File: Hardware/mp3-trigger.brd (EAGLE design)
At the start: 58.4 x 62.2 mm, 88 parts, among them IC1 LM1117, J1 POWER_JACKTOE, Q1 12.288MHz, U1 CY8C29466, U10 M18_, U2 USD-SOCKET, U3 MUX-74HC4067SMD, U5 1.8V Reg, U6 NAV_SWITCHSMD, U7 VS1063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

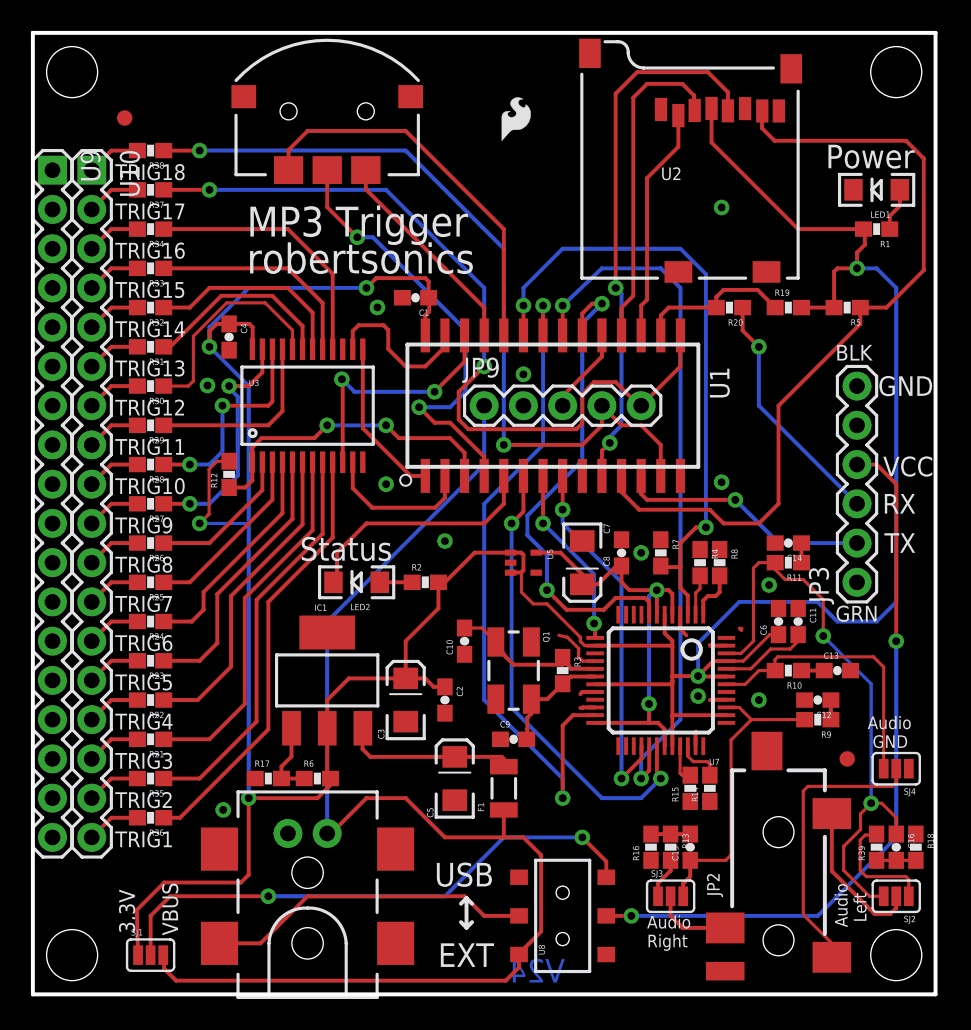
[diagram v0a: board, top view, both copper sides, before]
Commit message: Minor changes from Toni K review
Acid trap elimination, angles, added notes about jumpers, minor
rerouting.
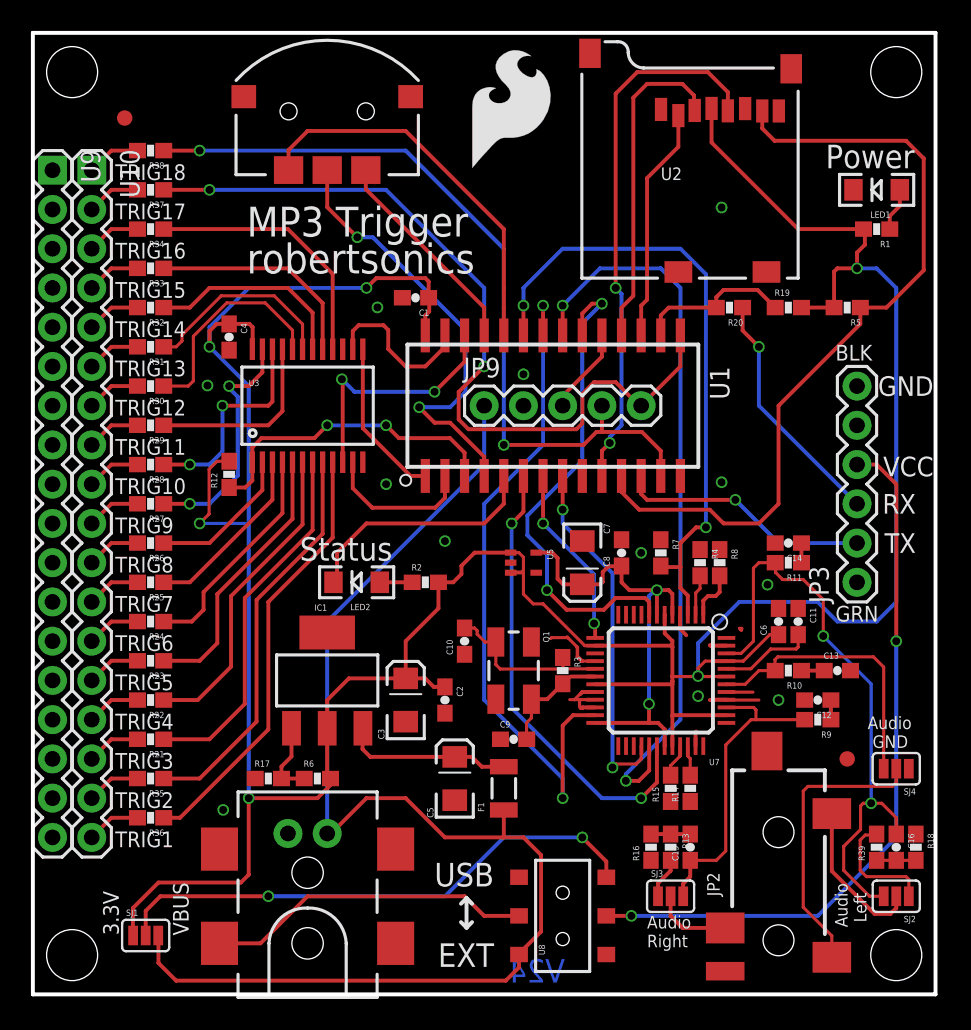
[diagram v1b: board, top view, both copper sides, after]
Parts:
- removed FRAME1: FRAME-LETTERNO_PACKAGE, SparkFun-Aesthetics:DUMMY
- removed U$3: LOGO-SFESK, SparkFun:SFE-LOGO-FLAME
- added LOGO1: SFE_LOGO_FLAME.3_INCH, SparkFun-Aesthetics:SFE_LOGO_FLAME_.3
- added U$4: REVISION, SparkFun-Aesthetics:REVISION
- JP6, JP7: device SparkFun:FIDUCIAL-1X2 -> SparkFun-Aesthetics:FIDUCIAL-1X2
- U$1: value LOGO-SFENEW -> SFE_LOGO_NAME_FLAME.2_INCH; device SparkFun:SFE-NEW-WEBLOGO -> SparkFun-Aesthetics:SFE_LOGO_NAME_FLAME_.2
- U$12, U$13, U$14, U$15: device SparkFun:STAND-OFF -> SparkFun-Electromechanical:STAND-OFF
- moved U$1 3.81 mm to (44.6, 47.1)
- moved SJ1 1.31 mm to (7.30, 3.81)
- moved R15 1.27 mm to (41.3, 13.3)
- moved R14 1.27 mm to (42.5, 13.3)
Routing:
- net GND: track 10.3 -> 20.5 mm
- net MSI: track 46.2 -> 47.8 mm
- net VBUS: track 82.4 -> 83.8 mm
- net CVDD: track 29.5 -> 30.6 mm
- net N$10: track 3.01 -> 1.95 mm
- net N$5: track 10.4 -> 11.3 mm
- net N$20: track 35.8 -> 35.0 mm
- net TRIG13: track 12.7 -> 13.4 mm
- net TRIG18: track 52.4 -> 51.7 mm
- net MSCLK: track 23.8 -> 23.1 mm
- net N$11: track 5.80 -> 6.44 mm
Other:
- board text added: "Joel Bartlett"
- board text removed: "Updated by: Joel Bartlett"

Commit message: Added OSHW Logo
Added OSHW Logo
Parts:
- added LOGO3: OSHW-LOGOM, SparkFun-Aesthetics:OSHW-LOGO-M

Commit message: QC Checklist Crrections
Minor error fixes
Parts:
- added FRAME1: FRAME-LETTERNO_PACKAGE, SparkFun-Aesthetics:DUMMY
- renumbered IC1 to U4
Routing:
- net GND: track 20.5 -> 18.7 mm

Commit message: Ready for reds
Added Input Voltages to silk, bumped up cream for solder jumpers,
centered logos on back.
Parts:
- moved LOGO3 5.16 mm to (28.6, 47.2)
- moved U$1 4.66 mm to (40.4, 49.1)
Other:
- board text added: "4.5 - 12V"
- board text added: "4.5-12V"
- board text added: "FTDI"
- board text added: "Input Voltage:"

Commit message: FTDI Silk update
Changed to 5V FTDI
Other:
- board text added: "5V FTDI"
- board text removed: "FTDI"
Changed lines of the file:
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@@
 <setting verticaltext="up"/>
 </settings>
-<grid distance="0.05" unitdist="inch" unit="inch" style="lines" multiple="1" display="yes" altdistance="0.001" altunitdist="inch" altunit="inch"/>
+<grid distance="0.05" unitdist="inch" unit="inch" style="lines" multiple="1" display="yes" altdistance="0.005" altunitdist="inch" altunit="inch"/>
 <layers>
 <layer number="1" name="Top" color="4" fill="1" visible="yes" active="yes"/>
@@
 <layer number="29" name="tStop" color="7" fill="3" visible="no" active="yes"/>
 <layer number="30" name="bStop" color="7" fill="6" visible="no" active="yes"/>
-<layer number="31" name="tCream" color="7" fill="4" visible="yes" active="yes"/>
+<layer number="31" name="tCream" color="7" fill="4" visible="no" active="yes"/>
 <layer number="32" name="bCream" color="7" fill="5" visible="no" active="yes"/>
 <layer number="33" name="tFinish" color="6" fill="3" visible="no" active="yes"/>
@@
 <layer number="47" name="Measures" color="7" fill="1" visible="no" active="yes"/>
 <layer number="48" name="Document" color="7" fill="1" visible="no" active="yes"/>
-<layer number="49" name="Reference" color="7" fill="1" visible="yes" active="yes"/>
+<layer number="49" name="Reference" color="7" fill="1" visible="no" active="yes"/>
 <layer number="50" name="dxf" color="7" fill="1" visible="no" active="yes"/>
 <layer number="51" name="tDocu" color="6" fill="1" visible="yes" active="yes"/>
@@
 <rectangle x1="7.0104" y1="2.3368" x2="8.7376" y2="2.921" layer="31"/>
 <rectangle x1="7.0104" y1="4.699" x2="8.7376" y2="5.2832" layer="31"/>
-<text x="51.3334" y="30.9118" size="1.4224" layer="21" font="vector" ratio="15" rot="R90">FTDI</text>
+<text x="51.2064" y="30.2768" size="1.4224" layer="21" font="vector" ratio="15" rot="R90">5V FTDI</text>
 </plain>
 <attributes>
